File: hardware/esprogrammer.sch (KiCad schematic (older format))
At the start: 25 parts, among them P1 USB_OTG, P2 CONN_02X03, Q1 MMBT3904, Q2 MMBT3904, SW1 SW_PUSH, SW2 SW_PUSH, U1 AP1117, U2 CP2102

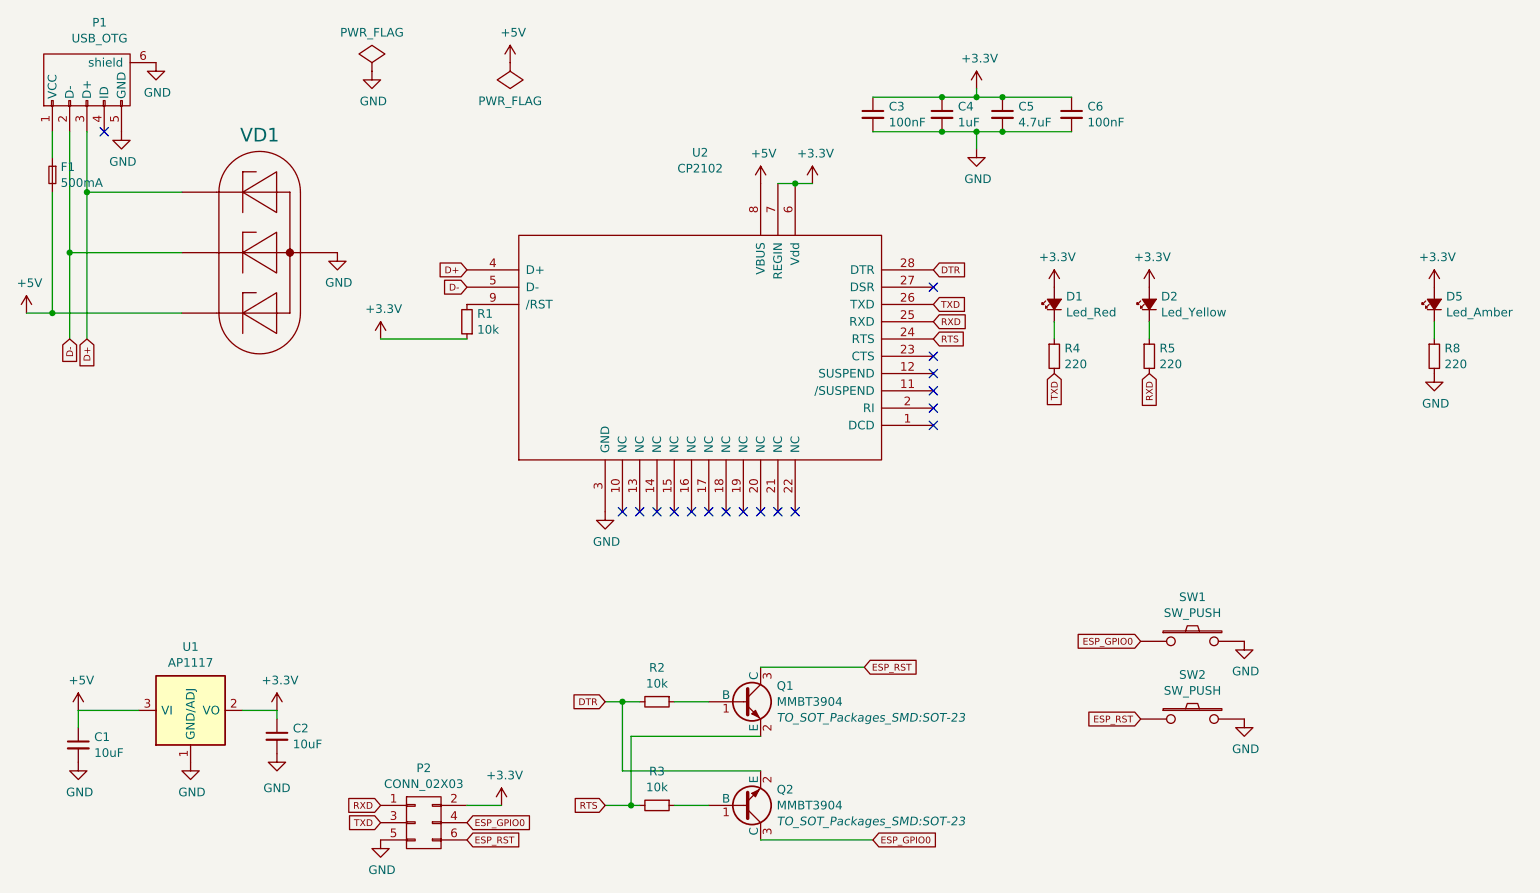
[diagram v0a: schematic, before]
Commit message: Programmer 0.6 - cleanup and use reflow size pads.
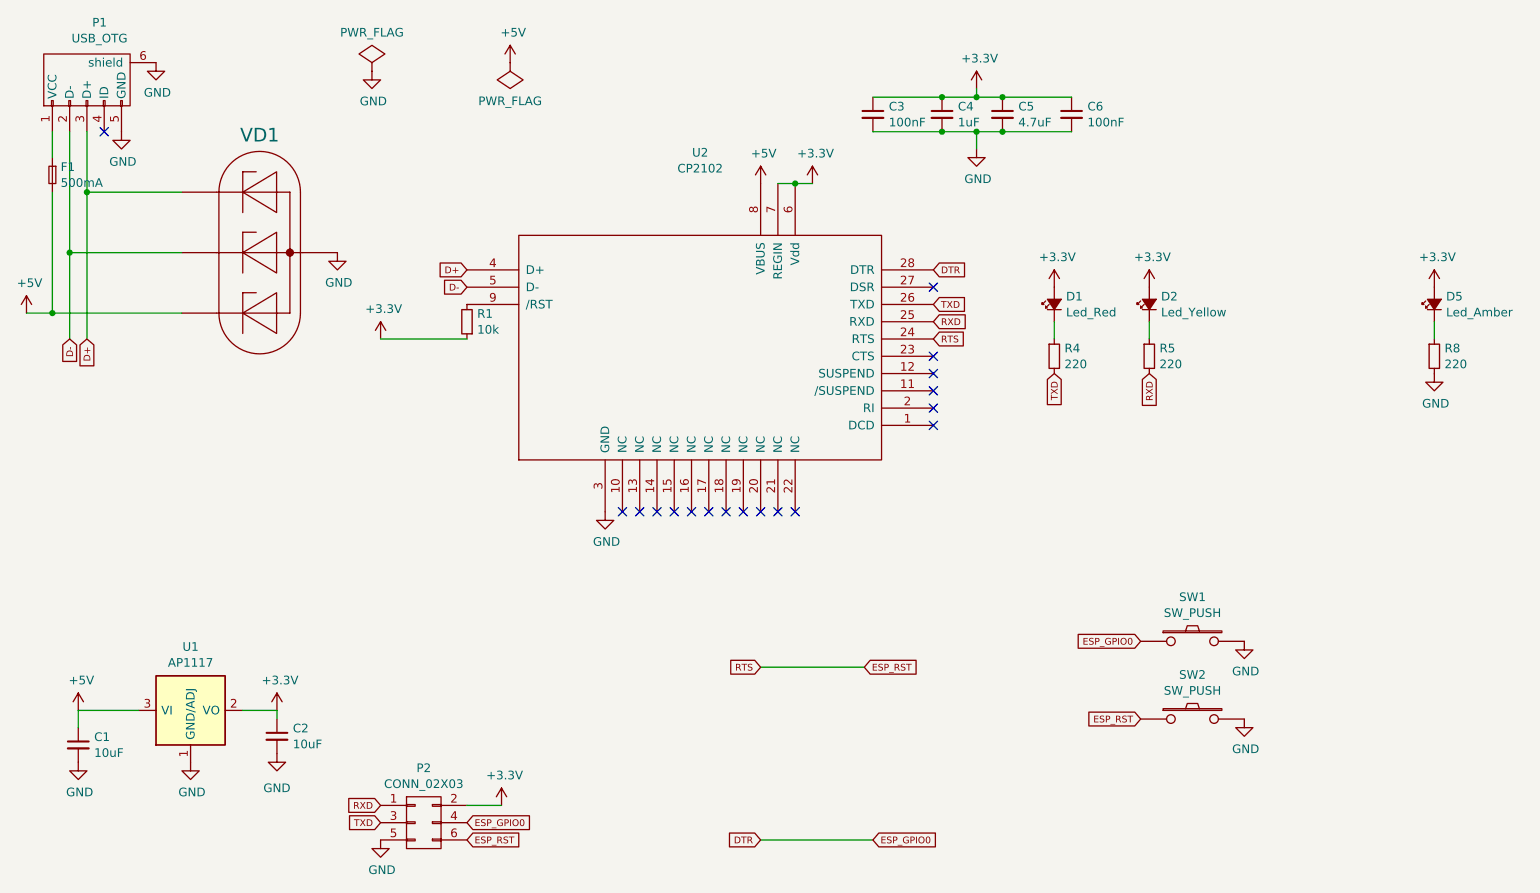
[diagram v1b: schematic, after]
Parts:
- removed Q1, Q2: MMBT3904, TO_SOT_Packages_SMD:SOT-23, symbol MMBT3904
- removed R2, R3: 10k, Resistors_SMD:R_0603_HandSoldering, symbol R_Small
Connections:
- net ESP_GPIO0 is gone; now on net DTR: P2.4 (P4), SW1.1
- net RTS is gone; now on net ESP_RST: U2.24 (RTS)
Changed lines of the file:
@@
 LIBS:esd
 LIBS:cp2102
+LIBS:esprogrammer-cache
 EELAYER 25 0
 EELAYER END
@@
 $EndComp
 $Comp
-L MMBT3904 Q2
-U 1 1 5758FD7F
-P 4800 5100
-F 0 "Q2" H 4993 5008 50  0000 L CNN
-F 1 "MMBT3904" H 4993 5100 50  0000 L CNN
-F 2 "TO_SOT_Packages_SMD:SOT-23" H 4993 5192 50  0000 L CIN
-F 3 "" H 4800 5100 50  0000 L CNN
-	1    4800 5100
-	1    0    0    1
-$EndComp
-$Comp
-L MMBT3904 Q1
-U 1 1 5758FDE9
-P 4800 4500
-F 0 "Q1" H 4993 4592 50  0000 L CNN
-F 1 "MMBT3904" H 4993 4500 50  0000 L CNN
-F 2 "TO_SOT_Packages_SMD:SOT-23" H 4993 4408 50  0000 L CIN
-F 3 "" H 4800 4500 50  0000 L CNN
-	1    4800 4500
-	1    0    0    -1
-$EndComp
-$Comp
-L R_Small R2
-U 1 1 5758FE3E
-P 4300 4500
-F 0 "R2" V 4103 4500 50  0000 C CNN
-F 1 "10k" V 4195 4500 50  0000 C CNN
-F 2 "Resistors_SMD:R_0603_HandSoldering" H 4300 4500 50  0001 C CNN
-F 3 "" H 4300 4500 50  0000 C CNN
-	1    4300 4500
-	0    1    1    0
-$EndComp
-$Comp
-L R_Small R3
-U 1 1 5758FEE0
-P 4300 5100
-F 0 "R3" V 4103 5100 50  0000 C CNN
-F 1 "10k" V 4195 5100 50  0000 C CNN
-F 2 "Resistors_SMD:R_0603_HandSoldering" H 4300 5100 50  0001 C CNN
-F 3 "" H 4300 5100 50  0000 C CNN
-	1    4300 5100
-	0    1    1    0
-$EndComp
-$Comp
 L CONN_02X03 P2
 U 1 1 57658F87
@@
 Text GLabel 5900 2300 2    39   Input ~ 0
 RXD
-Text GLabel 4000 4500 0    39   Input ~ 0
+Text GLabel 4900 5300 0    39   Input ~ 0
 DTR
-Text GLabel 4000 5100 0    39   Input ~ 0
+Text GLabel 4900 4300 0    39   Input ~ 0
 RTS
 Text GLabel 5500 4300 2    39   Input ~ 0
@@
 NoConn ~ 5100 3400
 Wire Wire Line
-	4400 4500 4600 4500
-Wire Wire Line
-	4400 5100 4600 5100
-Wire Wire Line
-	4000 4500 4200 4500
-Wire Wire Line
-	4000 5100 4200 5100
-Wire Wire Line
-	4900 4900 4100 4900
-Wire Wire Line
-	4100 4900 4100 4500
-Connection ~ 4100 4500
-Wire Wire Line
-	4900 4700 4150 4700
-Wire Wire Line
-	4150 4700 4150 5100
-Connection ~ 4150 5100
-Wire Wire Line
 	4900 4300 5500 4300
 Wire Wire Line
@@
 	800  1550 800  2250
 Wire Wire Line
-	650  2250 1550 2250
-Wire Wire Line
-	900  1200 900  2400
+	650  2250 800  2250
+Wire Wire Line
+	800  2250 1550 2250
+Wire Wire Line
+	900  1200 900  1900
+Wire Wire Line
+	900  1900 900  2400
 Wire Wire Line
 	900  1900 1550 1900
 Wire Wire Line
-	1000 1200 1000 2400
+	1000 1200 1000 1550
+Wire Wire Line
+	1000 1550 1000 2400
 Wire Wire Line
 	1000 1550 1550 1550
@@
 NoConn ~ 5900 2100
 Wire Wire Line
-	5000 1500 5200 1500
+	5000 1500 5100 1500
+Wire Wire Line
+	5100 1500 5200 1500
 Connection ~ 5100 1500
 $Comp
@@
 $EndComp
 Wire Wire Line
-	5550 1000 6700 1000
+	5550 1000 5950 1000
+Wire Wire Line
+	5950 1000 6150 1000
+Wire Wire Line
+	6150 1000 6300 1000
+Wire Wire Line
+	6300 1000 6700 1000
 Connection ~ 5950 1000
 Connection ~ 6300 1000
@@
 Connection ~ 6150 1000
 Wire Wire Line
-	5550 1200 6700 1200
+	5550 1200 5950 1200
+Wire Wire Line
+	5950 1200 6150 1200
+Wire Wire Line
+	6150 1200 6300 1200
+Wire Wire Line
+	6300 1200 6700 1200
 Connection ~ 5950 1200
 Connection ~ 6300 1200
